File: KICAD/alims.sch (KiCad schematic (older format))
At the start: 28 parts, among them U14 AD8030, U15 LT8365, U16 LM4040DBZ-2.5

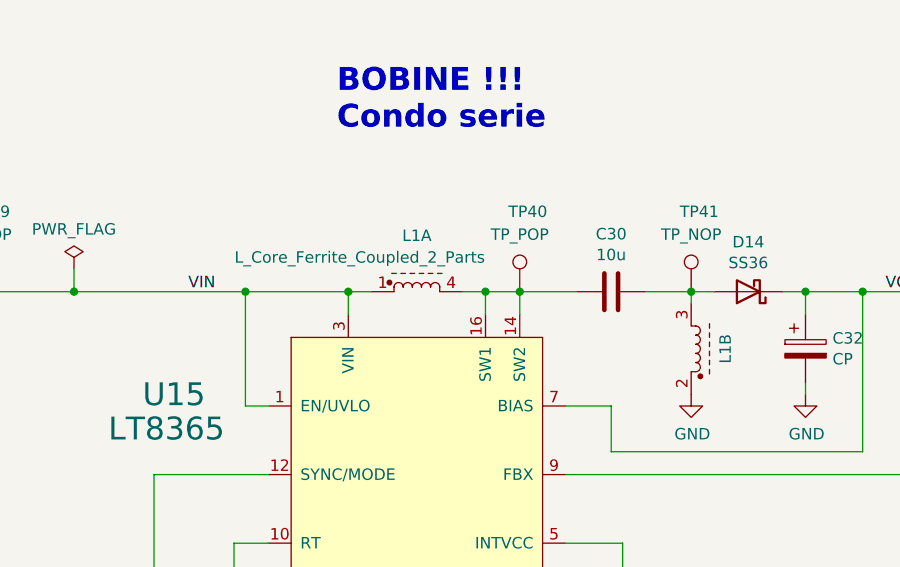
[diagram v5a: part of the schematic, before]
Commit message: added footprint for sepic coil + no more errors in netlist
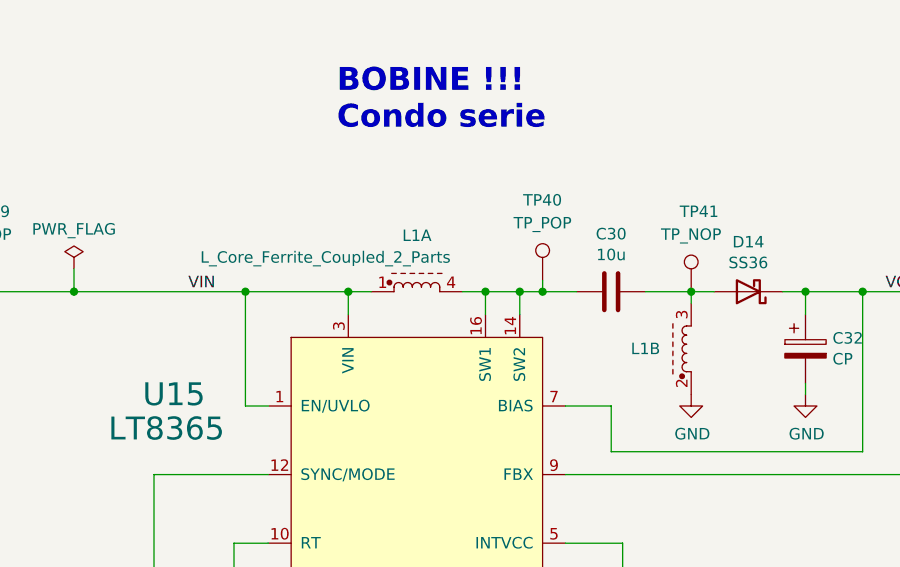
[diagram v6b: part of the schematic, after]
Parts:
- C27, C28, C29, C31: footprint Capacitor_SMD:C_0805_2012Metric_Pad1.15x1.40mm_HandSolder -> Sesame_footprint:C_0805_2012Metric_Pad1.18x1.45mm_HandSolder
- C32: footprint (none) -> Capacitor_SMD:C_Elec_4x5.8
- L1: footprint (none) -> Sesame_footprint:WE-DD_1260_128012
- R79, R80, R81, R82, R83, R84: footprint Resistor_SMD:R_0805_2012Metric_Pad1.15x1.40mm_HandSolder -> Sesame_footprint:R_0805_2012Metric_Pad1.20x1.40mm_HandSolder
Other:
- moved on the sheet: TP40
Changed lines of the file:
@@
 F 0 "R83" H 8870 2846 50  0000 L CNN
 F 1 "R" H 8870 2755 50  0000 L CNN
-F 2 "Resistor_SMD:R_0805_2012Metric_Pad1.15x1.40mm_HandSolder" V 8730 2800 50  0001 C CNN
+F 2 "Sesame_footprint:R_0805_2012Metric_Pad1.20x1.40mm_HandSolder" V 8730 2800 50  0001 C CNN
 F 3 "~" H 8800 2800 50  0001 C CNN
 	1    8800 2800
@@
 F 3 "" H 8800 2550 50  0001 C CNN
 	1    8800 2550
-	1    0    0    -1
-$EndComp
-$Comp
-L Sesame:L_Core_Ferrite_Coupled_2_Parts L1
-U 1 1 6123AB5D
-P 4850 2650
-F 0 "L1" H 4850 2895 50  0000 C CNN
-F 1 "L_Core_Ferrite_Coupled_2_Parts" H 4600 2800 50  0000 C CNN
-F 2 "" H 4850 2750 50  0001 C CNN
-F 3 "~" H 4850 2750 50  0001 C CNN
-	1    4850 2650
 	1    0    0    -1
 $EndComp
@@
 F 0 "R80" H 5320 4396 50  0000 L CNN
 F 1 "R" H 5320 4305 50  0000 L CNN
-F 2 "Resistor_SMD:R_0805_2012Metric_Pad1.15x1.40mm_HandSolder" V 5180 4350 50  0001 C CNN
+F 2 "Sesame_footprint:R_0805_2012Metric_Pad1.20x1.40mm_HandSolder" V 5180 4350 50  0001 C CNN
 F 3 "~" H 5250 4350 50  0001 C CNN
 	1    5250 4350
@@
 $EndComp
 Wire Wire Line
-	5550 2650 5300 2650
+	5550 2650 5400 2650
 Connection ~ 5300 2650
 Connection ~ 6550 2650
@@
 	-1   0    0    1
 $EndComp
-$Comp
-L Sesame:L_Core_Ferrite_Coupled_2_Parts L1
-U 2 1 6123D71D
-P 6050 2900
-F 0 "L1" H 6050 3050 50  0000 C CNN
-F 1 "L_Core_Ferrite_Coupled_2_Parts" V 6750 3000 50  0001 C CNN
-F 2 "" H 6050 3000 50  0001 C CNN
-F 3 "~" H 6050 3000 50  0001 C CNN
-	2    6050 2900
-	0    1    -1   0
-$EndComp
 Wire Wire Line
 	7200 3200 7200 3450
@@
 F 0 "R81" H 7270 3096 50  0000 L CNN
 F 1 "1M" H 7270 3005 50  0000 L CNN
-F 2 "Resistor_SMD:R_0805_2012Metric_Pad1.15x1.40mm_HandSolder" V 7130 3050 50  0001 C CNN
+F 2 "Sesame_footprint:R_0805_2012Metric_Pad1.20x1.40mm_HandSolder" V 7130 3050 50  0001 C CNN
 F 3 "~" H 7200 3050 50  0001 C CNN
 	1    7200 3050
@@
 F 0 "R82" H 7270 3896 50  0000 L CNN
 F 1 "296k" H 7270 3805 50  0000 L CNN
-F 2 "Resistor_SMD:R_0805_2012Metric_Pad1.15x1.40mm_HandSolder" V 7130 3850 50  0001 C CNN
+F 2 "Sesame_footprint:R_0805_2012Metric_Pad1.20x1.40mm_HandSolder" V 7130 3850 50  0001 C CNN
 F 3 "~" H 7200 3850 50  0001 C CNN
 	1    7200 3850
@@
 F 0 "C29" H 5365 4696 50  0000 L CNN
 F 1 "C" H 5365 4605 50  0000 L CNN
-F 2 "Capacitor_SMD:C_0805_2012Metric_Pad1.15x1.40mm_HandSolder" H 5288 4500 50  0001 C CNN
+F 2 "Sesame_footprint:C_0805_2012Metric_Pad1.18x1.45mm_HandSolder" H 5288 4500 50  0001 C CNN
 F 3 "~" H 5250 4650 50  0001 C CNN
 	1    5250 4650
@@
 F 0 "R79" H 4120 4546 50  0000 L CNN
 F 1 "84.5" H 4120 4455 50  0000 L CNN
-F 2 "Resistor_SMD:R_0805_2012Metric_Pad1.15x1.40mm_HandSolder" V 3980 4500 50  0001 C CNN
+F 2 "Sesame_footprint:R_0805_2012Metric_Pad1.20x1.40mm_HandSolder" V 3980 4500 50  0001 C CNN
 F 3 "~" H 4050 4500 50  0001 C CNN
 	1    4050 4500
@@
 F 0 "C28" H 4565 4546 50  0000 L CNN
 F 1 "C" H 4565 4455 50  0000 L CNN
-F 2 "Capacitor_SMD:C_0805_2012Metric_Pad1.15x1.40mm_HandSolder" H 4488 4350 50  0001 C CNN
+F 2 "Sesame_footprint:C_0805_2012Metric_Pad1.18x1.45mm_HandSolder" H 4488 4350 50  0001 C CNN
 F 3 "~" H 4450 4500 50  0001 C CNN
 	1    4450 4500
@@
 F 0 "C31" H 5865 4546 50  0000 L CNN
 F 1 "C" H 5865 4455 50  0000 L CNN
-F 2 "Capacitor_SMD:C_0805_2012Metric_Pad1.15x1.40mm_HandSolder" H 5788 4350 50  0001 C CNN
+F 2 "Sesame_footprint:C_0805_2012Metric_Pad1.18x1.45mm_HandSolder" H 5788 4350 50  0001 C CNN
 F 3 "~" H 5750 4500 50  0001 C CNN
 	1    5750 4500
@@
 F 0 "C27" H 1465 6996 50  0000 L CNN
 F 1 "100n" H 1465 6905 50  0000 L CNN
-F 2 "Capacitor_SMD:C_0805_2012Metric_Pad1.15x1.40mm_HandSolder" H 1388 6800 50  0001 C CNN
+F 2 "Sesame_footprint:C_0805_2012Metric_Pad1.18x1.45mm_HandSolder" H 1388 6800 50  0001 C CNN
 F 3 "~" H 1350 6950 50  0001 C CNN
 	1    1350 6950
@@
 L Connector:TestPoint TP?
 U 1 1 61530DA6
-P 5300 2650
+P 5400 2600
 AR Path="/614794AE/61530DA6" Ref="TP?"  Part="1"
 AR Path="/61456C6A/61530DA6" Ref="TP?"  Part="1"
 AR Path="/61530DA6" Ref="TP?"  Part="1"
 AR Path="/60F1AA92/61530DA6" Ref="TP40"  Part="1"
-F 0 "TP40" H 5250 3000 50  0000 L CNN
-F 1 "TP_POP" H 5300 2900 50  0000 C CNN
-F 2 "TestPoint:TestPoint_Loop_D1.80mm_Drill1.0mm_Beaded" H 5500 2650 50  0001 C CNN
-F 3 "~" H 5500 2650 50  0001 C CNN
-	1    5300 2650
+F 0 "TP40" H 5400 2950 50  0000 C CNN
+F 1 "TP_POP" H 5400 2850 50  0000 C CNN
+F 2 "TestPoint:TestPoint_Loop_D1.80mm_Drill1.0mm_Beaded" H 5600 2600 50  0001 C CNN
+F 3 "~" H 5600 2600 50  0001 C CNN
+	1    5400 2600
 	1    0    0    -1
 $EndComp
@@
 F 0 "R84" V 9943 3500 50  0000 C CNN
 F 1 "10k" V 10034 3500 50  0000 C CNN
-F 2 "Resistor_SMD:R_0805_2012Metric_Pad1.15x1.40mm_HandSolder" V 10080 3500 50  0001 C CNN
+F 2 "Sesame_footprint:R_0805_2012Metric_Pad1.20x1.40mm_HandSolder" V 10080 3500 50  0001 C CNN
 F 3 "~" H 10150 3500 50  0001 C CNN
 	1    10150 3500
@@
 F 0 "C32" H 6668 2946 50  0000 L CNN
 F 1 "CP" H 6668 2855 50  0000 L CNN
-F 2 "" H 6588 2750 50  0001 C CNN
+F 2 "Capacitor_SMD:C_Elec_4x5.8" H 6588 2750 50  0001 C CNN
 F 3 "~" H 6550 2900 50  0001 C CNN
 	1    6550 2900
 	1    0    0    -1
 $EndComp
+$Comp
+L Sesame:L_Core_Ferrite_Coupled_2_Parts L1
+U 1 1 61275E01
+P 4850 2650
+F 0 "L1" H 4850 2895 50  0000 C CNN
+F 1 "L_Core_Ferrite_Coupled_2_Parts" H 4450 2800 50  0000 C CNN
+F 2 "Sesame_footprint:WE-DD_1260_128012" H 4850 2750 50  0001 C CNN
+F 3 "~" H 4850 2750 50  0001 C CNN
+	1    4850 2650
+	1    0    0    -1
+$EndComp
+$Comp
+L Sesame:L_Core_Ferrite_Coupled_2_Parts L1
+U 2 1 61277F5C
+P 6050 2900
+F 0 "L1" V 6050 3100 50  0000 C CNN
+F 1 "L_Core_Ferrite_Coupled_2_Parts" H 5650 3050 50  0001 C CNN
+F 2 "Sesame_footprint:WE-DD_1260_128012" H 6050 3000 50  0001 C CNN
+F 3 "~" H 6050 3000 50  0001 C CNN
+	2    6050 2900
+	0    -1   -1   0
+$EndComp
+Wire Wire Line
+	5400 2600 5400 2650
+Connection ~ 5400 2650
+Wire Wire Line
+	5400 2650 5300 2650
 $EndSCHEMATC

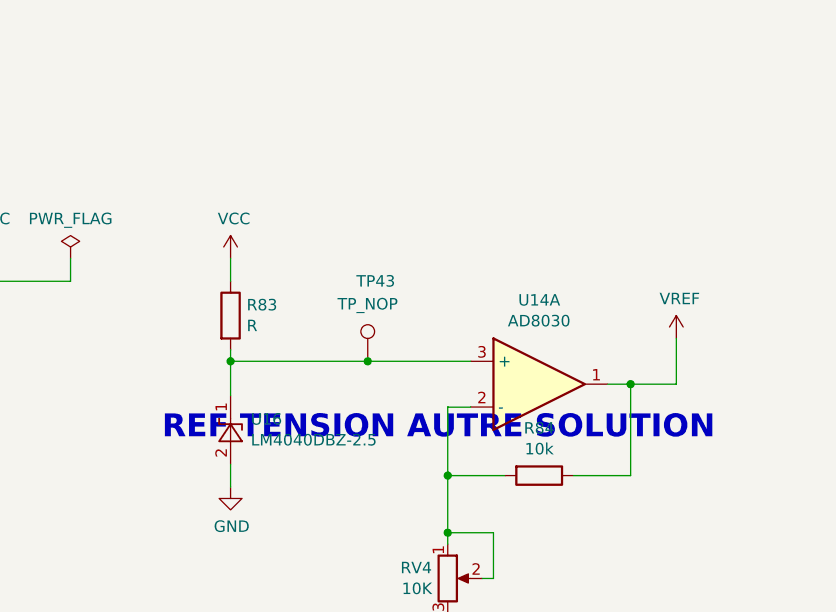
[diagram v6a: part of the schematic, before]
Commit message: added footprint sepic + place place place
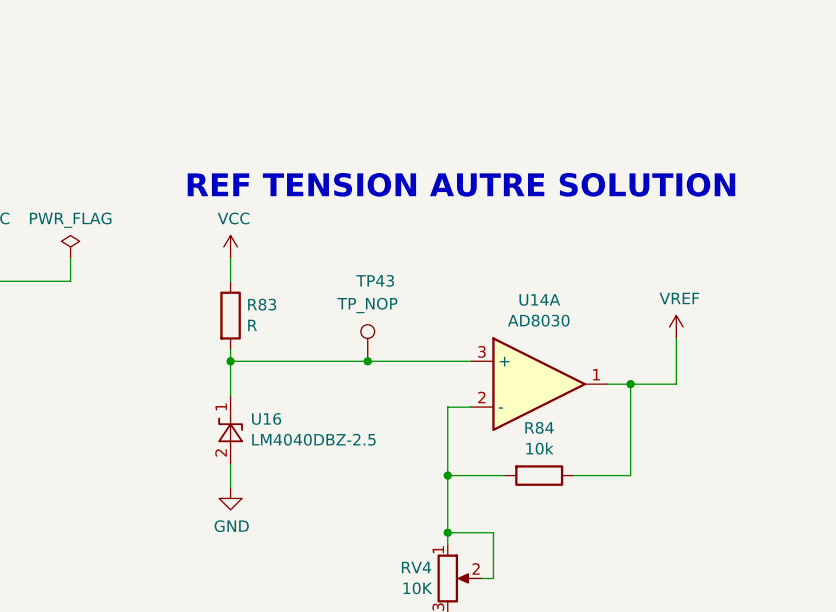
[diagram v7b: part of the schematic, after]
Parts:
- U15: footprint Package_SO:MSOP-16-1EP_3x4mm_P0.5mm_EP1.65x2.85mm_ThermalVias -> Sesame_footprint:MSE-16-1EP_3x4mm_P0.5mm_EP1.65x2.85mm_ThermalVias
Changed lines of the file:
@@
 F 0 "U15" H 3650 3700 100 0000 L CNN
 F 1 "LT8365" H 3500 3550 100 0000 L CNN
-F 2 "Package_SO:MSOP-16-1EP_3x4mm_P0.5mm_EP1.65x2.85mm_ThermalVias" H 4850 4100 100 0001 C CNN
+F 2 "Sesame_footprint:MSE-16-1EP_3x4mm_P0.5mm_EP1.65x2.85mm_ThermalVias" H 4850 4100 100 0001 C CNN
 F 3 "" H 4850 4100 100 0001 C CNN
 	1    4850 3400
@@
 Text Notes 4500 1950 0    100  ~ 20
 BOBINE !!!\nCondo serie
-Text Notes 8500 3350 0    100  ~ 20
+Text Notes 8600 2300 0    100  ~ 20
 REF TENSION AUTRE SOLUTION\n
 $Comp

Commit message: sim vref + djd write
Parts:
- removed JP15, JP16: Jumper_2_Bridged, Jumper:SolderJumper-2_P1.3mm_Bridged_Pad1.0x1.5mm, symbol Jumper:Jumper_2_Bridged
- removed R84: 10k, Sesame_footprint:R_0805_2012Metric_Pad1.20x1.40mm_HandSolder, symbol Device:R
- removed RV4: 10K, Potentiometer_SMD:Potentiometer_Bourns_3214W_Vertical, symbol Device:R_POT
- removed TP43, TP44: TP_NOP, TestPoint:TestPoint_THTPad_D2.0mm_Drill1.0mm, symbol Connector:TestPoint
- removed unit 1 of U14
- removed unit 2 of U14
- removed U16: LM4040DBZ-2.5, Package_TO_SOT_SMD:SOT-23, symbol Reference_Voltage:LM4040DBZ-2.5
- added R? (x2): R, Sesame_footprint:R_0805_2012Metric_Pad1.20x1.40mm_HandSolder, symbol Device:R
- added U?: TL431DBZ, Package_TO_SOT_SMD:SOT-23, symbol Reference_Voltage:TL431DBZ
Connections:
- net GND: now also R?.2, U?.3 (A)
- net VREF: now also R83.2, R?.1, U?.1 (K)
- new net: R?.1, R?.2, U?.2 (REF)
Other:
- moved on the sheet: R83
